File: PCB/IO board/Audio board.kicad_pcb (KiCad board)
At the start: 2 copper layers, 150 x 150 mm, 220 parts, among them J101 Screen_Standoff, J102 Screen_Standoff, J103 Standoff_MaGee, J104 Screen_Standoff, J105 Screen_Standoff, J301 6.3mm TRS, J501 Conn_01x02, J601 Jack-DC, J602 TEST_1P, J801 Conn_01x06_Male, Q201 BC846BPDW1, Q202 BC846BPDW1, Q501 NTGD3148N, SW701 SW_SPST, SW702 SW_SPST, SW703 SW_SPST, U201 MCP634, U202 74LVC2G66DC,125, U203 74LVC2G66DC,125, U301 TLV9064, U401 MCP6002-xSN, U402 TPS61170, U501 PAM2401, U502 AP9101C, U503 DIO5158, U601 TPS54332, U602 MIC23050, U801 ESP32S, U802 ESP32, X101 Cap'n_MaGee, X201 XLR/6.3Combo, X202 XLR/6.3Combo, X203 SJ1-3525N, X301 SJ1-3525N

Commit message: PCB Backup
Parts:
- added R728: 12k, Resistors_SMD:R_0603, F.Cu at (35.5, 151.6)
- added R729: 12k, Resistors_SMD:R_0603, F.Cu at (102.7, 150.1)
- added R730: 12k, Resistors_SMD:R_0603, F.Cu at (161.8, 153.7)
- C212, C215: moved to B.Cu
- U501: footprint Housings_SSOP:MSOP-8-1EP_3x3mm_Pitch0.65mm -> Housings_SSOP:MSOP-8_3x3mm_Pitch0.65mm
- moved R721 337.0 mm to (163.8, 153.1), turned to 180 degrees
- moved R718 327.3 mm to (153.4, 134.4)
- moved R715 326.1 mm to (155.3, 133.9), turned to 90 degrees
- moved R712 325.7 mm to (159.8, 153.7), turned to 90 degrees
- moved R724 320.1 mm to (162.9, 169.1), turned to 180 degrees
- moved R706 319.5 mm to (162.3, 133.9), turned to 90 degrees
- moved R727 318.9 mm to (160.9, 168.6), turned to 90 degrees
- moved R703 317.5 mm to (164.3, 134.4), turned to 180 degrees
- moved R709 310.6 mm to (157.8, 153.7), turned to 90 degrees
- moved C709 276.0 mm to (163.2, 155.3), turned to 270 degrees
- moved R720 274.5 mm to (101.3, 150.1), turned to 270 degrees
- moved C703 274.4 mm to (160.2, 133.3)
- moved C706 273.2 mm to (157.4, 133.3), turned to 180 degrees
- moved C712 273.1 mm to (160.9, 165.9), turned to 90 degrees
- moved R705 263.9 mm to (102.7, 137.8), turned to 270 degrees
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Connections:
- R719 pad 2: ENCODER_1_SW -> Net-(R719-Pad2)
- R720 pad 2: ENCODER_2_SW -> Net-(R720-Pad2)
- R721 pad 2: ENCODER_3_SW -> Net-(R721-Pad2)
- R802 pad 1: Net-(R802-Pad1) -> +3V3
- R802 pad 2: +3V3 -> Net-(R801-Pad2)
- S701 pad 4: ENCODER_1_SW -> Net-(R719-Pad2)
- S702 pad 4: ENCODER_2_SW -> Net-(R720-Pad2)
- S703 pad 4: ENCODER_3_SW -> Net-(R721-Pad2)
- S801 pad 3: Net-(R802-Pad1) -> Net-(S801-Pad3)
- U801 pad 10: BLUE_1 -> Phantom_2
- U801 pad 11: ORANGE_1 -> Phantom_1
- U801 pad 12: BLUE_2 -> Phantom
- U801 pad 13: ORANGE_2 -> ORANGE_3
- U801 pad 16: ORANGE_3 -> ORANGE_2
- U801 pad 17: Net-(U801-Pad17) -> BLUE_2
- U801 pad 29: Phantom -> Net-(U801-Pad29)
- U801 pad 30: Phantom_2 -> Net-(U801-Pad30)
- U801 pad 31: Phantom_1 -> ORANGE_1
- U801 pad 33: Net-(U801-Pad33) -> BLUE_1
- U802 pad 10: ORANGE_1 -> Phantom_1
- U802 pad 11: BLUE_2 -> Phantom
- U802 pad 12: ORANGE_2 -> ORANGE_3
- U802 pad 15: ORANGE_3 -> ORANGE_2
- U802 pad 16: Net-(U802-Pad16) -> BLUE_2
- U802 pad 29: Phantom -> Net-(U802-Pad29)
- U802 pad 30: Phantom_2 -> Net-(U802-Pad30)
- U802 pad 31: Phantom_1 -> ORANGE_1
- U802 pad 33: Net-(U802-Pad33) -> BLUE_1
- U802 pad 9: BLUE_1 -> Phantom_2
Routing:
- net GND: track 0.00 -> 445.1 mm, vias 0 -> 151
- net +5V: track 0.00 -> 323.9 mm, vias 0 -> 4
- net +3V3: track 0.00 -> 240.3 mm, vias 0 -> 4
- net +5V_AUX: track 0.00 -> 222.1 mm, vias 0 -> 10
- net Net-(Q201-Pad3): track 0.00 -> 193.0 mm, vias 0 -> 2
- net Net-(C604-Pad1): track 0.00 -> 186.1 mm, vias 0 -> 25
- net +1V65_Inputs: track 0.00 -> 173.4 mm
- net Net-(Q202-Pad3): track 0.00 -> 150.9 mm, vias 0 -> 2
- net +1V65_Outputs: track 0.00 -> 124.8 mm
- net +5V_USB: track 0.00 -> 111.7 mm, vias 0 -> 6
- net +5V_BAT: track 0.00 -> 103.1 mm, vias 0 -> 13
- net Net-(C305-Pad2): track 0.00 -> 92.0 mm, vias 0 -> 2
- net DAC1+: track 0.00 -> 91.6 mm, vias 0 -> 4
- net DAC1-: track 0.00 -> 83.8 mm, vias 0 -> 2
- net Net-(C308-Pad2): track 0.00 -> 80.1 mm, vias 0 -> 2
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- added copper zone on F.Cu, net +5V_AUX
- added copper zone on B.Cu, net GND

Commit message: IO board Rev 1.0 RC-1
Board for inspection by Supervisor
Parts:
- added G***: LOGO, CTAG:CTAG, B.Cu at (163.2, 122.3)
- added REF**: Fiducial_1mm_Dia_2.54mm_Outer_CopperTop, Fiducials:Fiducial_1mm_Dia_2.54mm_Outer_CopperTop, F.Cu at (166.6, 30.5)
- added REF**: Fiducial_1mm_Dia_2.54mm_Outer_CopperTop, Fiducials:Fiducial_1mm_Dia_2.54mm_Outer_CopperTop, F.Cu at (166.6, 176.7)
- added REF**: Fiducial_1mm_Dia_2.54mm_Outer_CopperTop, Fiducials:Fiducial_1mm_Dia_2.54mm_Outer_CopperTop, F.Cu at (20.4, 176.7)
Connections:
- J801 pad 4: ENCODER_1_A -> ENCODER_1_B
- J801 pad 5: ENCODER_1_B -> ENCODER_1_A
- X101 pad 21: Pad_2 -> Pad_1
- X101 pad 22: Impedance_2 -> Impedance_1
- X101 pad 23: Pad_1 -> Pad_2
- X101 pad 24: Impedance_1 -> Impedance_2
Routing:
- net +3V3: track 240.3 -> 565.8 mm, vias 4 -> 10
- net ENCODER_1_B: track 1.39 -> 117.9 mm, vias 0 -> 9
- net Pad_2: track 0.96 -> 112.3 mm, vias 1 -> 10
- net SW_3: track 1.17 -> 109.4 mm, vias 0 -> 10
- net ENCODER_3_SW: track 1.41 -> 106.9 mm, vias 0 -> 4
- net Impedance_2: track 0.90 -> 106.0 mm, vias 1 -> 10
- net ORANGE_3: track 8.47 -> 110.1 mm, vias 0 -> 2
- net BLUE_3: track 9.90 -> 110.1 mm, vias 0 -> 2
- net Pad_1: track 0.96 -> 98.2 mm, vias 1 -> 8
- net ENCODER_1_SW: track 1.66 -> 98.7 mm, vias 0 -> 9
- net Impedance_1: track 0.90 -> 94.1 mm, vias 1 -> 8
- net ENCODER_3_A: track 1.41 -> 91.8 mm, vias 0 -> 10
- net ENCODER_1_A: track 1.39 -> 89.6 mm, vias 0 -> 5
- net ENCODER_3_B: track 1.41 -> 87.9 mm, vias 0 -> 8
- net SW_1: track 1.41 -> 78.0 mm, vias 0 -> 12
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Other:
- board text added: "CTAG"
- board text added: "I/O"
- board text added: "Rev 1.0"
- board text added: "by Jesse Spiessens"
- board text removed: "Cap'n Magee"
- board text removed: "Screen"

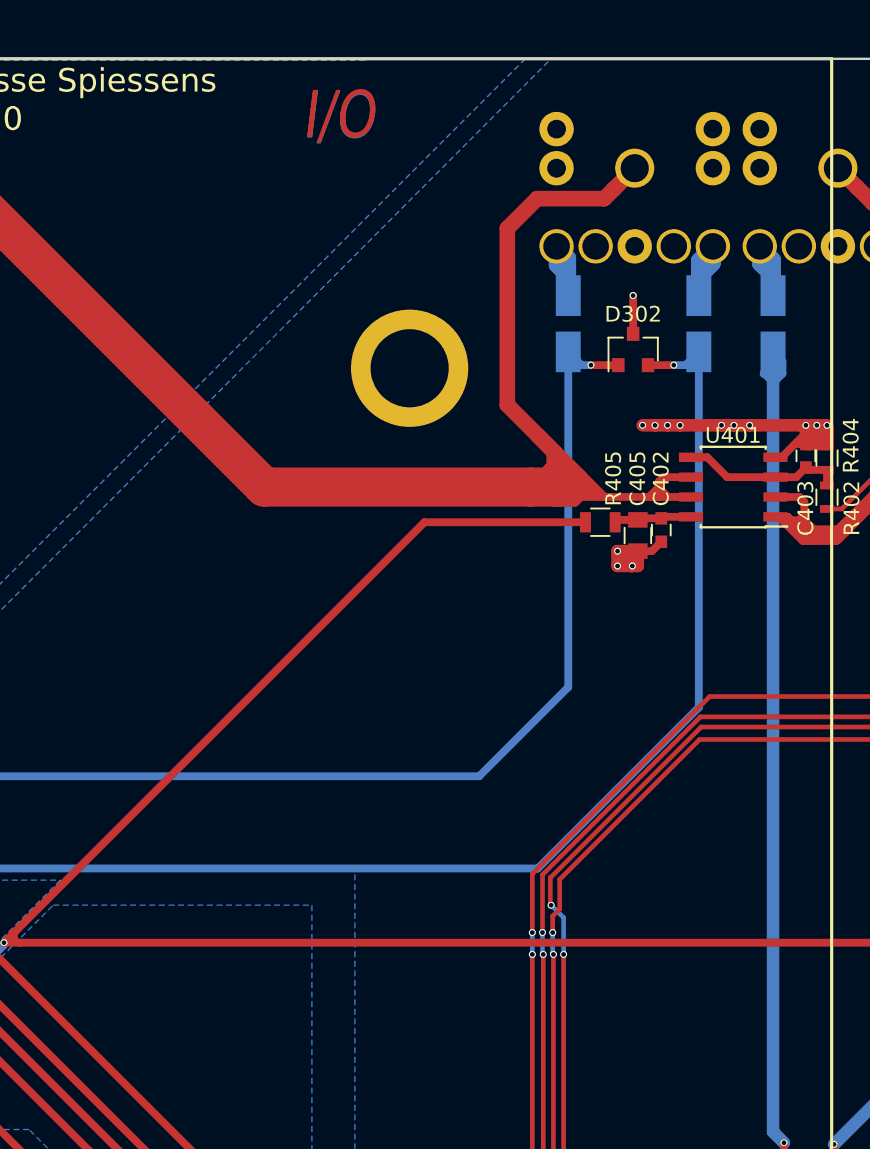
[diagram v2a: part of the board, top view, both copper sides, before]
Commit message: IO Rev 1.0 RC2 + Gerbers
ESP antenna keepout added
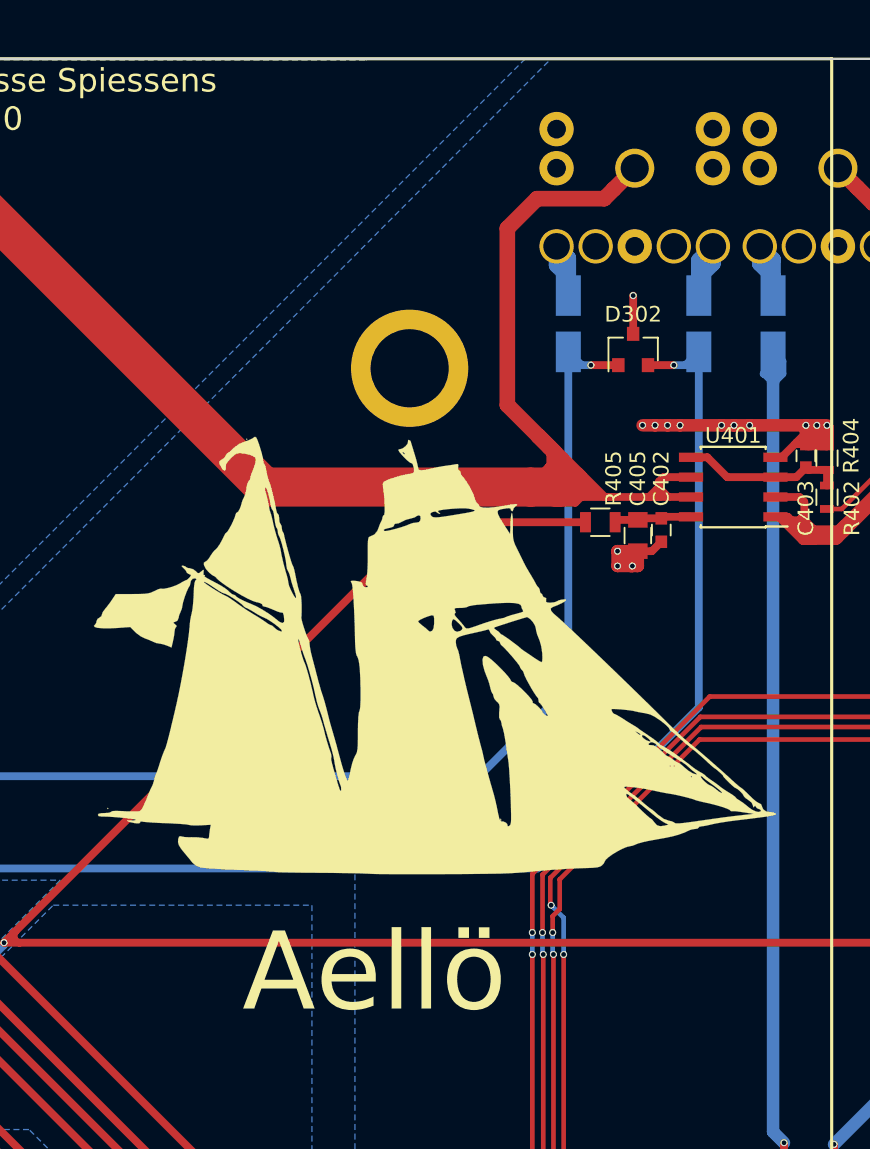
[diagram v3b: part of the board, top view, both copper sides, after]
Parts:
- added G***: LOGO, Graphics:Logo_IO, F.Cu at (84.2, 67.0)
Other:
- board text added: "Aellö"
- board text removed: "I/O"
